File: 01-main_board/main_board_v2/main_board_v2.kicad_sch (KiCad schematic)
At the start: 4 parts, among them J1 Mezzanine Edge, J4 DB44 (Analog | Digital)

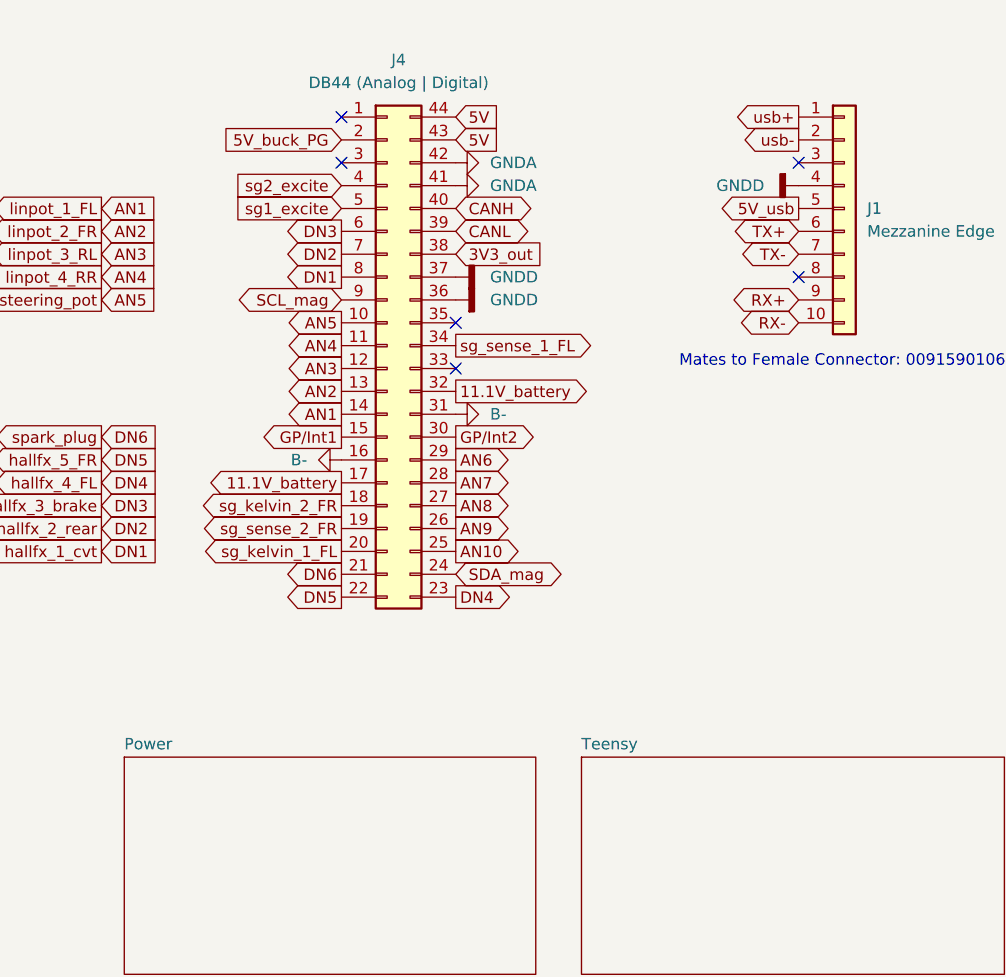
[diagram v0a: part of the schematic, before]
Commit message: changed 5v_ref, updated db44, reset pcb layout
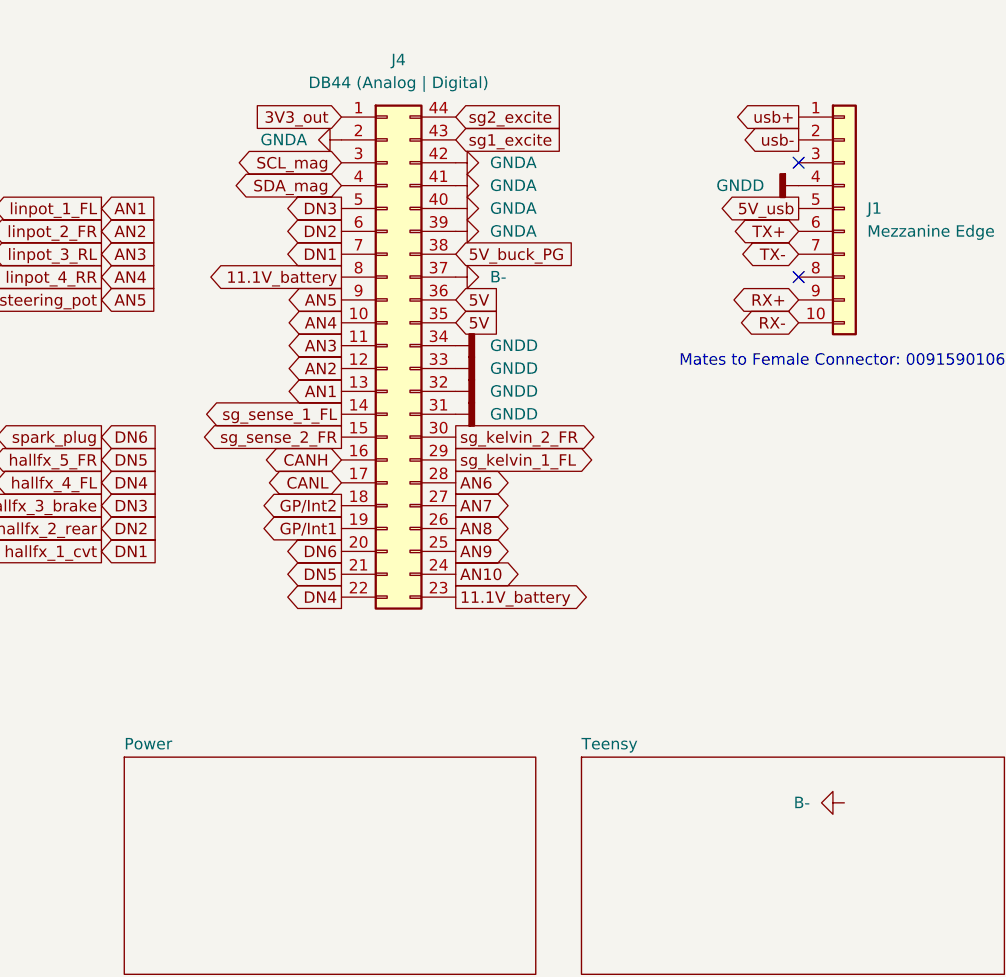
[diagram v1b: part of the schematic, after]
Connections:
- net 11.1V_battery: now also J4.23 (Pin_23), J4.8 (Pin_8); no longer J4.17 (Pin_17), J4.32 (Pin_32)
- net 3V3_out: now also J4.1 (Pin_1); no longer J4.38 (Pin_38)
- net 5V: now also J4.35 (Pin_35), J4.36 (Pin_36); no longer J4.43 (Pin_43), J4.44 (Pin_44)
- net 5V_buck_PG: now also J4.38 (Pin_38); no longer J4.2 (Pin_2)
- net AN1: now also J4.13 (Pin_13); no longer J4.14 (Pin_14)
- net AN10: now also J4.24 (Pin_24); no longer J4.25 (Pin_25)
- net AN2: now also J4.12 (Pin_12); no longer J4.13 (Pin_13)
- net AN3: now also J4.11 (Pin_11); no longer J4.12 (Pin_12)
- net AN4: now also J4.10 (Pin_10); no longer J4.11 (Pin_11)
- net AN5: now also J4.9 (Pin_9); no longer J4.10 (Pin_10)
- net AN6: now also J4.28 (Pin_28); no longer J4.29 (Pin_29)
- net AN7: now also J4.27 (Pin_27); no longer J4.28 (Pin_28)
- net AN8: now also J4.26 (Pin_26); no longer J4.27 (Pin_27)
- net AN9: now also J4.25 (Pin_25); no longer J4.26 (Pin_26)
- net B-: now also J4.37 (Pin_37); no longer J4.16 (Pin_16), J4.31 (Pin_31)
- net CANH: now also J4.16 (Pin_16); no longer J4.40 (Pin_40)
- net CANL: now also J4.17 (Pin_17); no longer J4.39 (Pin_39)
- net DN1: now also J4.7 (Pin_7); no longer J4.8 (Pin_8)
- net DN2: now also J4.6 (Pin_6); no longer J4.7 (Pin_7)
- net DN3: now also J4.5 (Pin_5); no longer J4.6 (Pin_6)
- net DN4: now also J4.22 (Pin_22); no longer J4.23 (Pin_23)
- net DN5: now also J4.21 (Pin_21); no longer J4.22 (Pin_22)
- net DN6: now also J4.20 (Pin_20); no longer J4.21 (Pin_21)
- net GNDA: now also J4.2 (Pin_2), J4.39 (Pin_39), J4.40 (Pin_40)
- net GNDD: now also J4.31 (Pin_31), J4.32 (Pin_32), J4.33 (Pin_33), J4.34 (Pin_34); no longer J4.36 (Pin_36), J4.37 (Pin_37)
- net GP/Int1: now also J4.19 (Pin_19); no longer J4.15 (Pin_15)
- net GP/Int2: now also J4.18 (Pin_18); no longer J4.30 (Pin_30)
- net SCL_mag: now also J4.3 (Pin_3); no longer J4.9 (Pin_9)
- net SDA_mag: now also J4.4 (Pin_4); no longer J4.24 (Pin_24)
- net sg1_excite: now also J4.43 (Pin_43); no longer J4.5 (Pin_5)
- net sg2_excite: now also J4.44 (Pin_44); no longer J4.4 (Pin_4)
- net sg_kelvin_1_FL: now also J4.29 (Pin_29); no longer J4.20 (Pin_20)
- net sg_kelvin_2_FR: now also J4.30 (Pin_30); no longer J4.18 (Pin_18)
- net sg_sense_1_FL: now also J4.14 (Pin_14); no longer J4.34 (Pin_34)
- net sg_sense_2_FR: now also J4.15 (Pin_15); no longer J4.19 (Pin_19)
- no-connect marks 6 -> 2

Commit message: made progress on layout
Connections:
- net usb_mux_s: now reaches J1.3 (Pin_3)
- net 5V_buck_PG renamed 5V_ref
- no-connect marks 2 -> 1
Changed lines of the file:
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@@
-	)
-	(no_connect
-		(at 111.76 38.1)
 	)
 	(no_connect
@@
 		)
 	)
+	(global_label "usb_mux_s"
+		(shape input)
+		(at 111.76 38.1 180)
+		(fields_autoplaced yes)
+		(effects
+			(font
+				(size 1.27 1.27)
+			)
+			(justify right)
+		)
+		(property "Intersheetrefs" "${INTERSHEET_REFS}"
+			(at 98.615 38.1 0)
+			(effects
+				(font
+					(size 1.27 1.27)
+				)
+				(justify right)
+				(hide yes)
+			)
+		)
+	)
 	(global_label "DN6"
 		(shape output)
@@
 		)
 	)
-	(global_label "5V_buck_PG"
+	(global_label "5V_ref"
 		(shape input)
 		(at 73.66 48.26 0)
@@
 		)
 		(property "Intersheetrefs" "${INTERSHEET_REFS}"
-			(at 87.8332 48.26 0)
+			(at 82.5114 48.26 0)
 			(effects
 				(font
@@
 					(unit 1)
 				)
-			)
-		)
-	)
-	(symbol
-		(lib_id "power:GNDA")
-		(at 116.84 109.22 270)
-		(unit 1)
-		(exclude_from_sim no)
-		(in_bom yes)
-		(on_board yes)
-		(dnp no)
-		(fields_autoplaced yes)
-		(property "Reference" "#PWR079"
-			(at 110.49 109.22 0)
-			(effects
-				(font
-					(size 1.27 1.27)
-				)
-				(hide yes)
-			)
-		)
-		(property "Value" "B-"
-			(at 113.03 109.2199 90)
-			(effects
-				(font
-					(size 1.27 1.27)
-				)
-				(justify right)
-			)
-		)
-		(property "Footprint" ""
-			(at 116.84 109.22 0)
-			(effects
-				(font
-					(size 1.27 1.27)
-				)
-				(hide yes)
-			)
-		)
-		(property "Datasheet" ""
-			(at 116.84 109.22 0)
-			(effects
-				(font
-					(size 1.27 1.27)
-				)
-				(hide yes)
-			)
-		)
-		(property "Description" "Power symbol creates a global label with name \"GNDA\" , analog ground"
-			(at 116.84 109.22 0)
-			(effects
-				(font
-					(size 1.27 1.27)
-				)
-				(hide yes)
-			)
-		)
-		(pin "1"
-		)
-		(instances
-			(project "main_board_v2"
-				(path "/12c2237c-5932-49af-9119-92b28c846ae7"
-					(reference "#PWR079")
-					(unit 1)
-				)

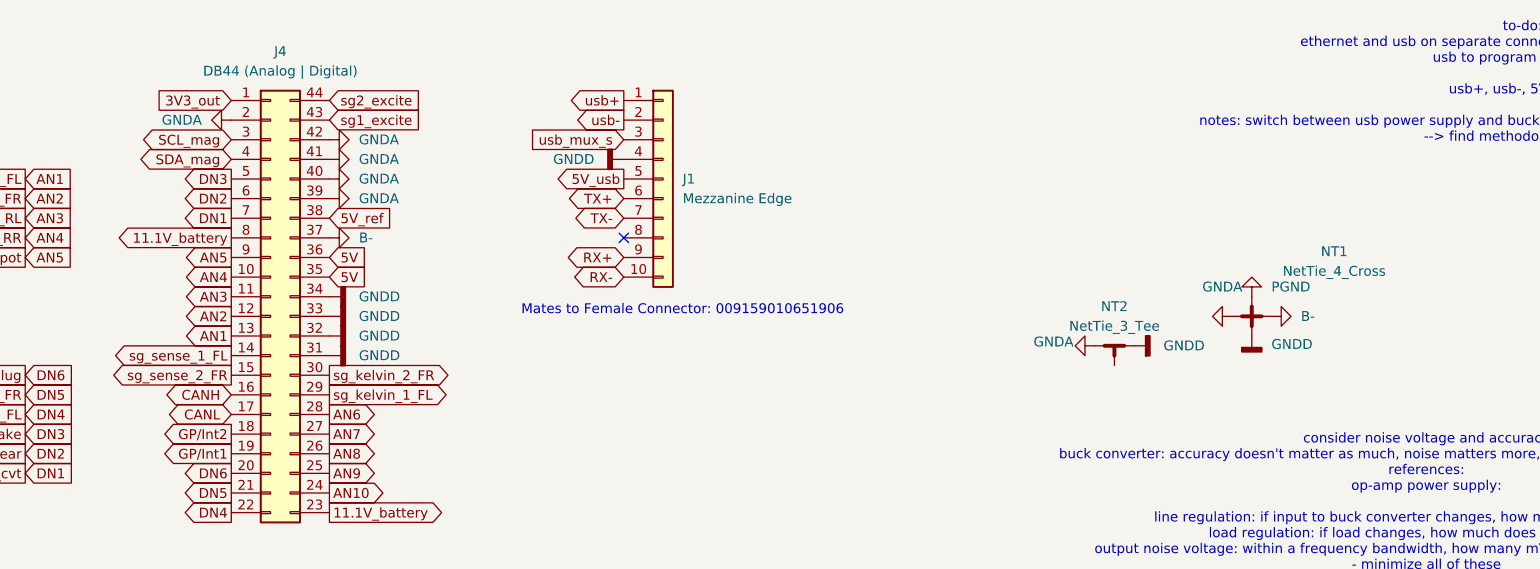
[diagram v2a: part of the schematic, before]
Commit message: changed buck converter, finished ground + power plane layout
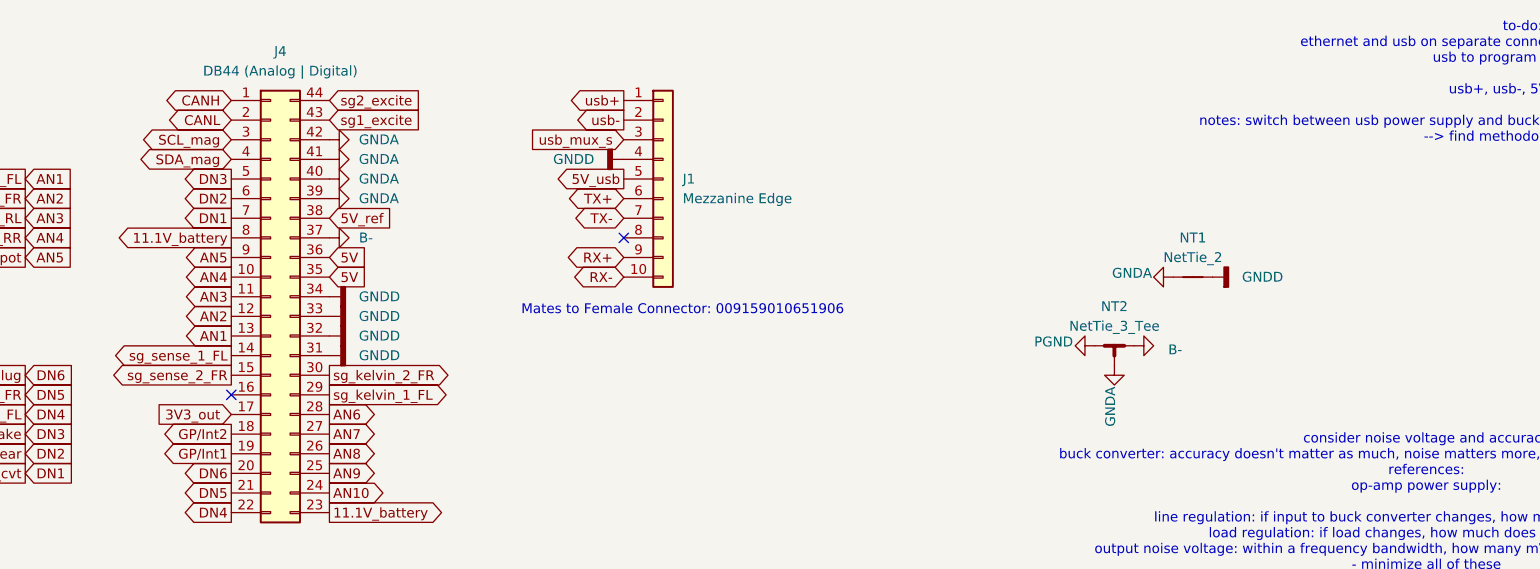
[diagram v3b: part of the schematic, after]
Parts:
- removed NT1: NetTie_4_Cross, NetTie:NetTie-4_SMD_Pad0.5mm, symbol Device:NetTie_4_Cross
- added NT1: NetTie_2, NetTie:NetTie-2_SMD_Pad0.5mm, symbol Device:NetTie_2
- NT2: footprint NetTie:NetTie-2_SMD_Pad0.5mm -> NetTie:NetTie-3_SMD_Pad0.5mm
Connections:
- net 3V3_out: now also J4.17 (Pin_17); no longer J4.1 (Pin_1)
- net B-: now also NT2.2
- net CANH: now also J4.1 (Pin_1); no longer J4.16 (Pin_16)
- net CANL: now also J4.2 (Pin_2); no longer J4.17 (Pin_17)
- net GNDA: now also NT2.3, NT1.1; no longer J4.2 (Pin_2), NT2.1
- net GNDD: now also NT1.2; no longer NT2.2
- net PGND: now also NT2.1
- no-connect marks 1 -> 2

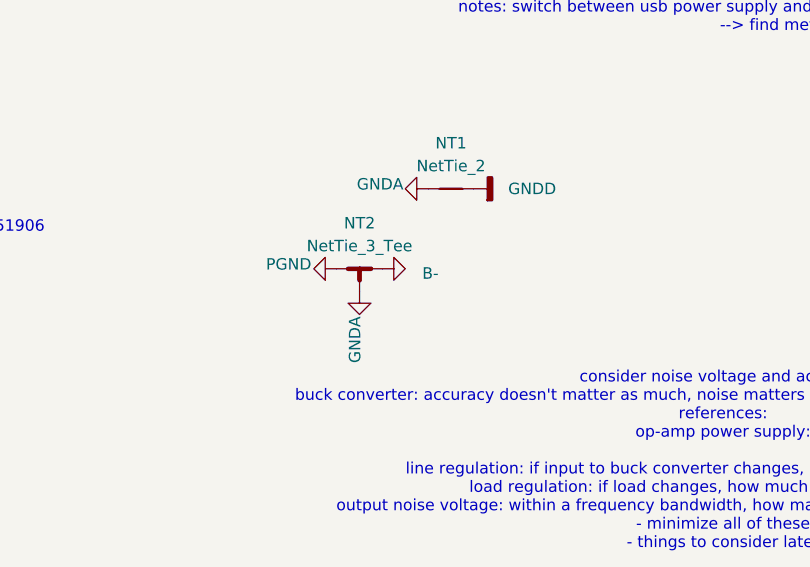
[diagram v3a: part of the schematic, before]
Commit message: finished sensor input layout and some spi bus
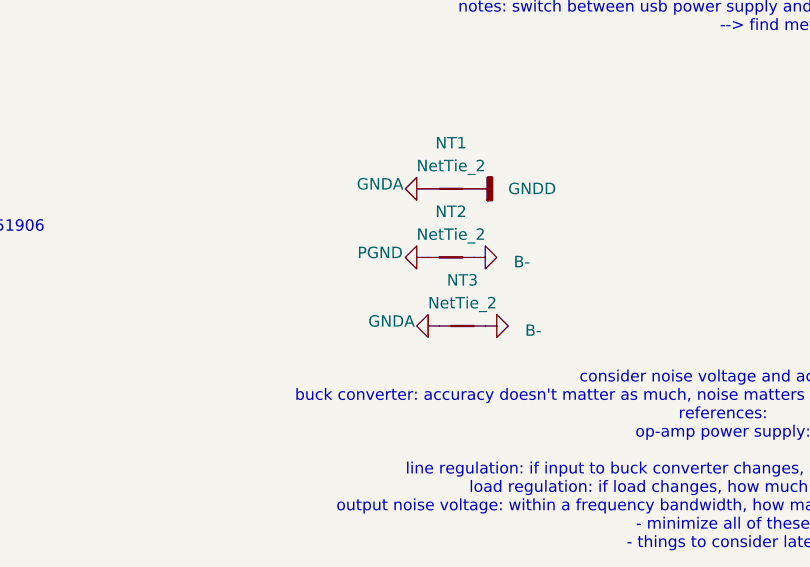
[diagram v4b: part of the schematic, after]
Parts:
- removed NT2: NetTie_3_Tee, NetTie:NetTie-3_SMD_Pad0.5mm, symbol Device:NetTie_3_Tee
- added NT2, NT3: NetTie_2, NetTie:NetTie-2_SMD_Pad0.5mm, symbol Device:NetTie_2
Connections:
- net B-: now also NT2.2, NT3.2
- net GNDA: now also NT3.1
- net PGND: now also NT2.1

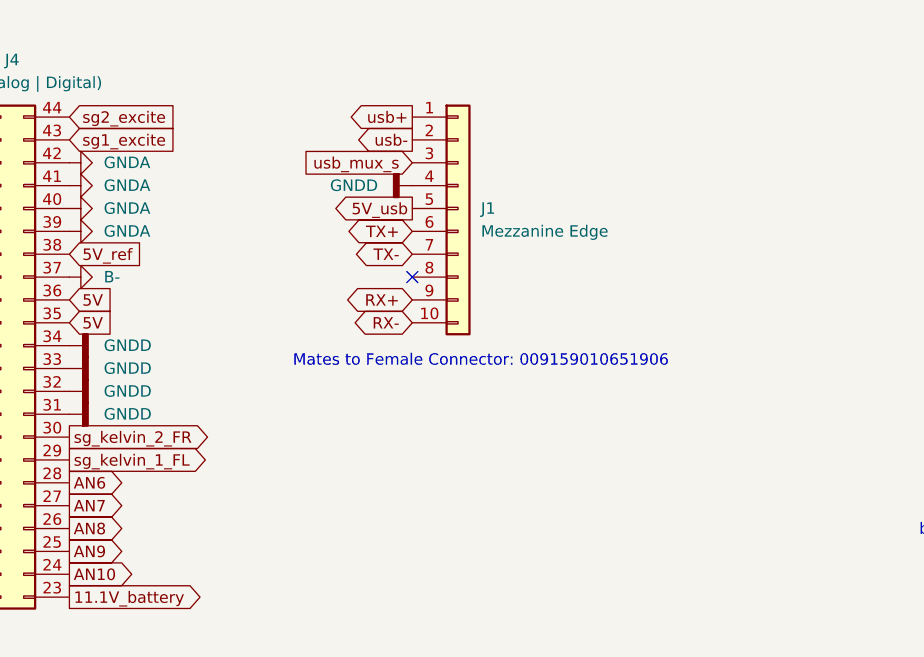
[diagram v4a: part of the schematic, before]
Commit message: finished layout, resolved drc errors, need to resolve warnings and get checked
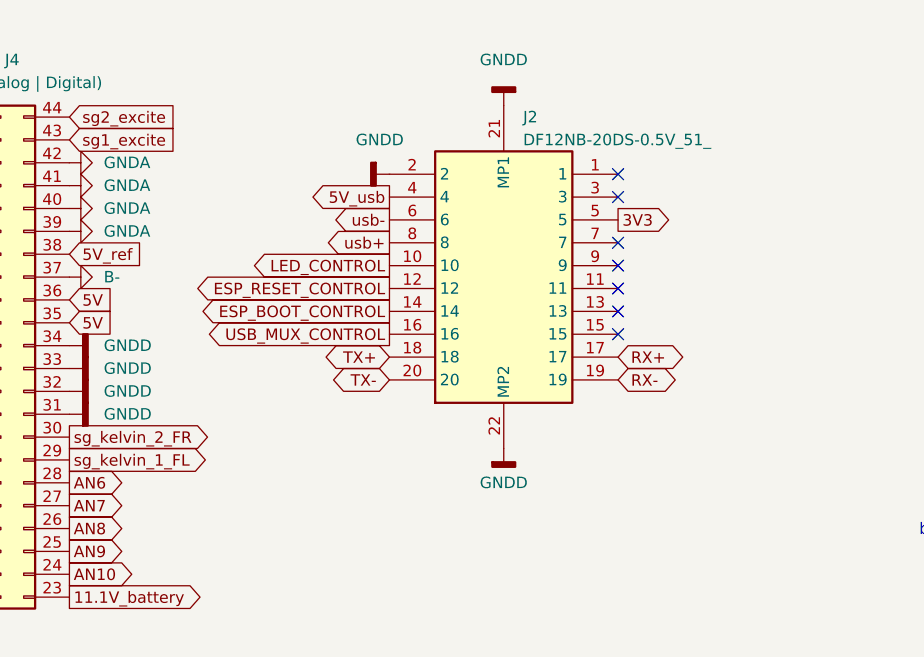
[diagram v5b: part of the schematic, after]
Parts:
- removed J1: Mezzanine Edge, 22XT_Main:Double Sided Mezzanine Card Edge_Edge Side, symbol Connector_Generic:Conn_01x10
- added J2: DF12NB-20DS-0.5V_51_, DF12NB20DS05V51, symbol 22XT_Main_v2:DF12NB-20DS-0.5V_51_
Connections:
- net 5V_usb: now also J2.4
- net GNDD: now also J2.2, J2.21 (MP1), J2.22 (MP2)
- net RX+: now also J2.17
- net RX-: now also J2.19
- net TX+: now also J2.18
- net TX-: now also J2.20
- net usb+: now also J2.8
- net usb-: now also J2.6
- new net 3V3: J2.5
- new net ESP_BOOT_CONTROL: J2.14
- new net ESP_RESET_CONTROL: J2.12
- new net LED_CONTROL: J2.10
- new net USB_MUX_CONTROL: J2.16
- no-connect marks 2 -> 8
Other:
- note removed: "Mates to Female Connector: 009159010651906"

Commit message: Finished preliminary routing
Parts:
- added H1, H2, H3, H4: MountingHole, MountingHole:MountingHole_3.2mm_M3_Pad, symbol Mechanical:MountingHole
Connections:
- net CANH renamed CAN+
- net CANL renamed CAN-
